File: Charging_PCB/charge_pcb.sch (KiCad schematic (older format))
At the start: 36 parts, among them J1 PCB_1, J2 Battery, J3 Power Switch, J4 24V Out, J5 Motor_Left, J6 Motor_Cutter, J7 Motor_Right, Q1 BC547C, Q2 IRF9540N, Q3 BC547C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

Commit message: Improve Q2 and Q4
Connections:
- net at D2.2 (K), R1.1, R4.1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: now also Q2.3 (S); no longer Q2.2 (D)
- net at D3.1 (K), U1.5 (IP-): now also Q2.2 (D); no longer Q2.3 (S)
- net at D5.2 (K), R6.1: now also Q4.3 (S); no longer Q4.2 (D)
- net at C1.1, J4.1, J5.1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: now also Q4.2 (D); no longer Q4.3 (S)
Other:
- moved on the sheet: Q2, Q4
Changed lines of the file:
@@
 Wire Wire Line
 	3500 2650 3500 2700
-Wire Wire Line
-	3500 2250 4400 2250
 Connection ~ 3500 2250
 $Comp
@@
 $EndComp
 Connection ~ 3500 3700
-Wire Wire Line
-	4400 2750 4850 2750
 Wire Wire Line
 	5500 3700 5500 3550
@@
 Wire Wire Line
 	4850 3000 4850 2750
-Connection ~ 4850 2750
 Wire Wire Line
 	4850 2750 5500 2750
@@
 L Transistor_FET:IRF9540N Q4
 U 1 1 60AF8999
-P 9000 2350
-F 0 "Q4" V 9342 2350 50  0000 C CNN
-F 1 "IRF9540N" V 9251 2350 50  0000 C CNN
-F 2 "Package_TO_SOT_THT:TO-220-3_Vertical" H 9200 2275 50  0001 L CIN
-F 3 "http://www.irf.com/product-info/datasheets/data/irf9540n.pdf" H 9000 2350 50  0001 L CNN
-	1    9000 2350
-	0    -1   -1   0
-$EndComp
-Wire Wire Line
-	7950 2550 7950 2950
-Wire Wire Line
-	9000 2550 7950 2550
-Connection ~ 7950 2550
+P 9000 2150
+F 0 "Q4" V 9342 2150 50  0000 C CNN
+F 1 "IRF9540N" V 9251 2150 50  0000 C CNN
+F 2 "Package_TO_SOT_THT:TO-220-3_Vertical" H 9200 2075 50  0001 L CIN
+F 3 "http://www.irf.com/product-info/datasheets/data/irf9540n.pdf" H 9000 2150 50  0001 L CNN
+	1    9000 2150
+	0    1    1    0
+$EndComp
+Wire Wire Line
+	7950 2550 7950 2600
 $Comp
 L Transistor_FET:IRF9540N Q2
 U 1 1 60B073F2
-P 4300 2550
-F 0 "Q2" H 4504 2596 50  0000 L CNN
-F 1 "IRF9540N" H 4504 2505 50  0000 L CNN
-F 2 "Package_TO_SOT_THT:TO-220-3_Vertical" H 4500 2475 50  0001 L CIN
-F 3 "http://www.irf.com/product-info/datasheets/data/irf9540n.pdf" H 4300 2550 50  0001 L CNN
-	1    4300 2550
-	1    0    0    -1
-$EndComp
-Wire Wire Line
-	4400 2250 4400 2350
-Wire Wire Line
-	4100 2650 4100 2550
+P 4500 2650
+F 0 "Q2" H 4704 2696 50  0000 L CNN
+F 1 "IRF9540N" H 4704 2605 50  0000 L CNN
+F 2 "Package_TO_SOT_THT:TO-220-3_Vertical" H 4700 2575 50  0001 L CIN
+F 3 "http://www.irf.com/product-info/datasheets/data/irf9540n.pdf" H 4500 2650 50  0001 L CNN
+	1    4500 2650
+	0    -1   -1   0
+$EndComp
 Wire Wire Line
 	6550 3050 6550 4650
@@
 Text GLabel 5500 6050 1    50   Output ~ 0
 pinBatteryVoltage
+Wire Wire Line
+	4700 2250 4700 2550
+Wire Wire Line
+	3500 2250 4700 2250
+Wire Wire Line
+	4300 2550 4300 2750
+Wire Wire Line
+	4300 2750 4850 2750
+Connection ~ 4850 2750
+Wire Wire Line
+	4100 2650 4100 2850
+Wire Wire Line
+	4100 2850 4500 2850
+Wire Wire Line
+	9000 1950 8400 1950
+Wire Wire Line
+	8400 1950 8400 2600
+Wire Wire Line
+	8400 2600 7950 2600
+Connection ~ 7950 2600
+Wire Wire Line
+	7950 2600 7950 2950
 $EndSCHEMATC

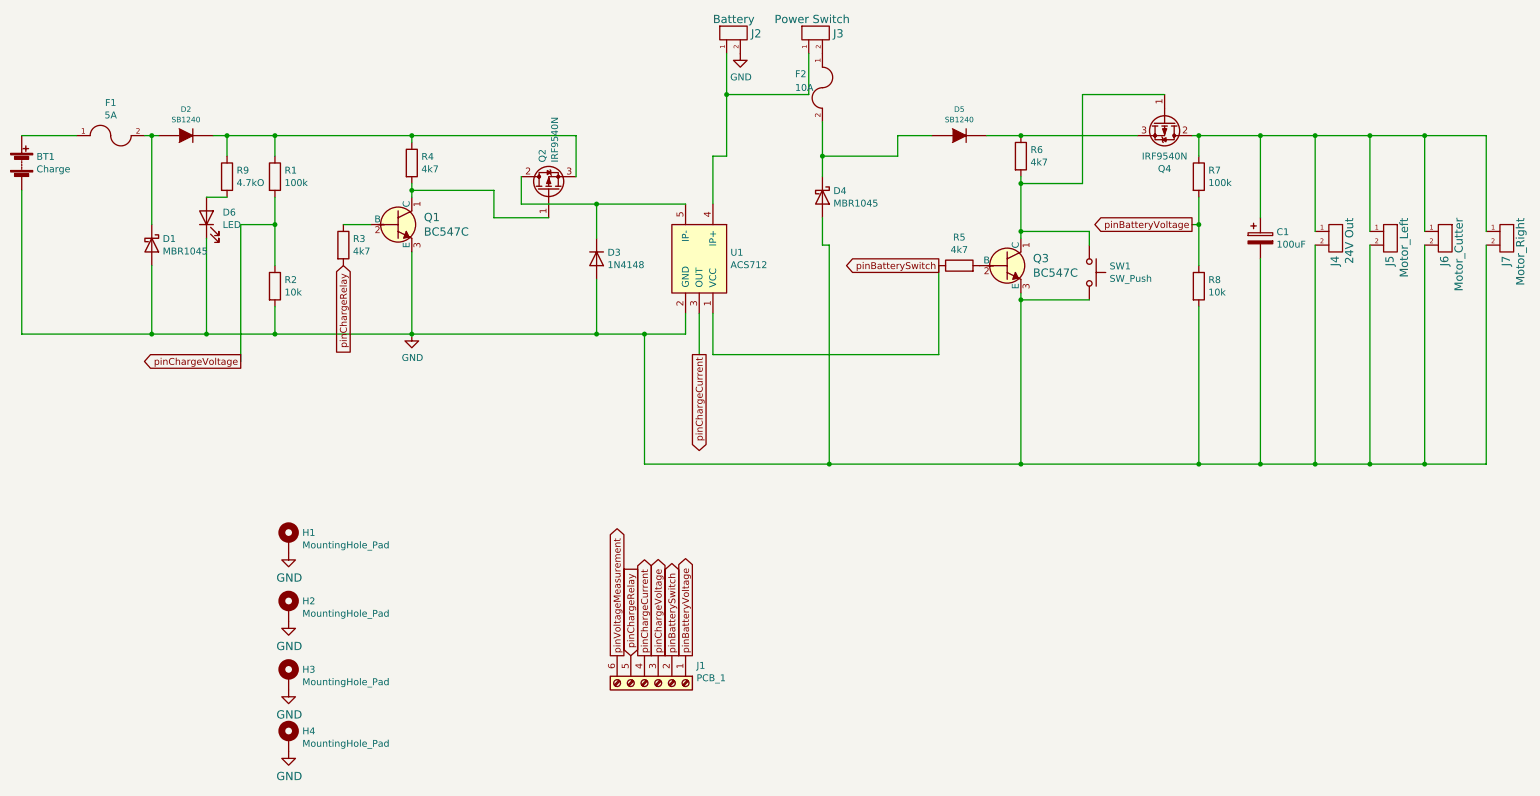
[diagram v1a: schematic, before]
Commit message: Rename pinChargeRelay to pinChargeEnable
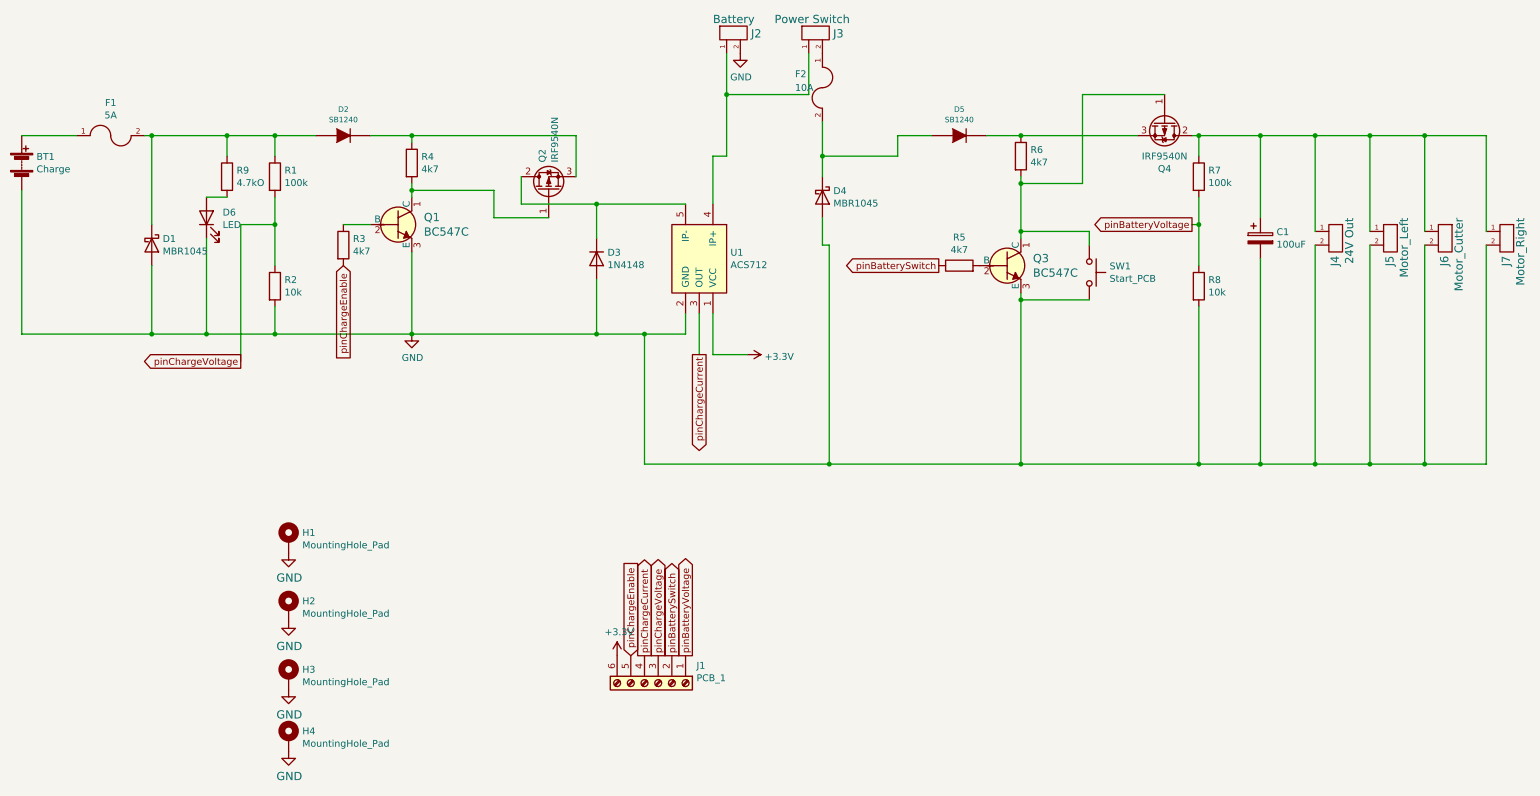
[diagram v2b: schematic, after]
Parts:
- SW1: value SW_Push -> Start_PCB
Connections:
- net pinBatterySwitch: no longer U1.1 (VCC)
- net at D1.1 (K), D2.1 (A), F1.2: now also R1.1, R9.1
- net at D2.2 (K), Q2.3 (S), R4.1: no longer R1.1, R9.1
- net pinChargeRelay renamed pinChargeEnable
- net pinVoltageMeasurement renamed +3V3
- net +3V3: now also U1.1 (VCC)
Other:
- moved on the sheet: D2
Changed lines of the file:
@@
 L Lötpad_2,5mm:DIODE D2
 U 1 1 6071023D
-P 1850 2250
-F 0 "D2" H 1850 2442 40  0000 C CNN
-F 1 "SB1240" H 1850 2366 40  0000 C CNN
-F 2 "Diode_THT:D_DO-41_SOD81_P10.16mm_Horizontal" H 1850 2250 60  0001 C CNN
-F 3 "" H 1850 2250 60  0000 C CNN
-	1    1850 2250
+P 3000 2250
+F 0 "D2" H 3000 2442 40  0000 C CNN
+F 1 "SB1240" H 3000 2366 40  0000 C CNN
+F 2 "Diode_THT:D_DO-41_SOD81_P10.16mm_Horizontal" H 3000 2250 60  0001 C CNN
+F 3 "" H 3000 2250 60  0000 C CNN
+	1    3000 2250
 	1    0    0    -1
 $EndComp
@@
 	3000 2900 3200 2900
 Text GLabel 3000 3200 3    50   Input ~ 0
-pinChargeRelay
+pinChargeEnable
 Wire Wire Line
 	3500 2650 4100 2650
@@
 Text GLabel 5400 6050 1    50   Output ~ 0
 pinBatterySwitch
-Text GLabel 5000 6050 1    50   Output ~ 0
-pinVoltageMeasurement
 Text GLabel 5200 6050 1    50   Output ~ 0
 pinChargeCurrent
 Text GLabel 5100 6050 1    50   Input ~ 0
-pinChargeRelay
+pinChargeEnable
 Wire Wire Line
 	650  2250 1050 2250
 Wire Wire Line
-	2500 2250 3500 2250
+	2500 2250 2800 2250
 $Comp
 L Lötpad_2,5mm:DIODE D5
@@
 Wire Wire Line
 	2250 2900 2500 2900
-Wire Wire Line
-	2050 2250 2150 2250
 Wire Wire Line
 	2150 2400 2150 2250
@@
 Wire Wire Line
 	650  3700 1600 3700
-Wire Wire Line
-	1600 2250 1650 2250
 $Comp
 L Switch:SW_Push SW1
@@
 P 8450 3250
 F 0 "SW1" V 8404 3398 50  0000 L CNN
-F 1 "SW_Push" V 8495 3398 50  0000 L CNN
+F 1 "Start_PCB" V 8495 3398 50  0000 L CNN
 F 2 "Connector_JST:JST_XH_B2B-XH-A_1x02_P2.50mm_Vertical" H 8450 3450 50  0001 C CNN
 F 3 "~" H 8450 3450 50  0001 C CNN
@@
 Wire Wire Line
 	7950 2950 7950 3000
-Wire Wire Line
-	7350 3850 7350 3200
-Wire Wire Line
-	5700 3850 7350 3850
 $Comp
 L Transistor_FET:IRF9540N Q4
@@
 Wire Wire Line
 	7950 2600 7950 2950
+$Comp
+L power:+3.3V #PWR?
+U 1 1 60A5AE88
+P 5000 6050
+F 0 "#PWR?" H 5000 5900 50  0001 C CNN
+F 1 "+3.3V" H 5015 6223 50  0000 C CNN
+F 2 "" H 5000 6050 50  0001 C CNN
+F 3 "" H 5000 6050 50  0001 C CNN
+	1    5000 6050
+	1    0    0    -1
+$EndComp
+$Comp
+L power:+3.3V #PWR?
+U 1 1 60A5B730
+P 5950 3850
+F 0 "#PWR?" H 5950 3700 50  0001 C CNN
+F 1 "+3.3V" V 5965 3978 50  0000 L CNN
+F 2 "" H 5950 3850 50  0001 C CNN
+F 3 "" H 5950 3850 50  0001 C CNN
+	1    5950 3850
+	0    1    1    0
+$EndComp
+Wire Wire Line
+	5700 3850 5950 3850
+Wire Wire Line
+	3200 2250 3500 2250
+Wire Wire Line
+	1600 2250 2150 2250
 $EndSCHEMATC

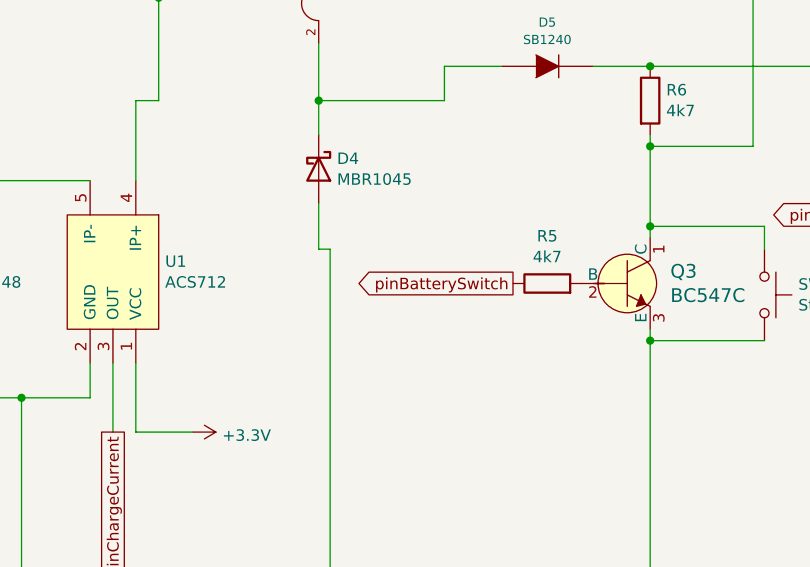
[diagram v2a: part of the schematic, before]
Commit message: Board Route
Board routed and make Gerber Files
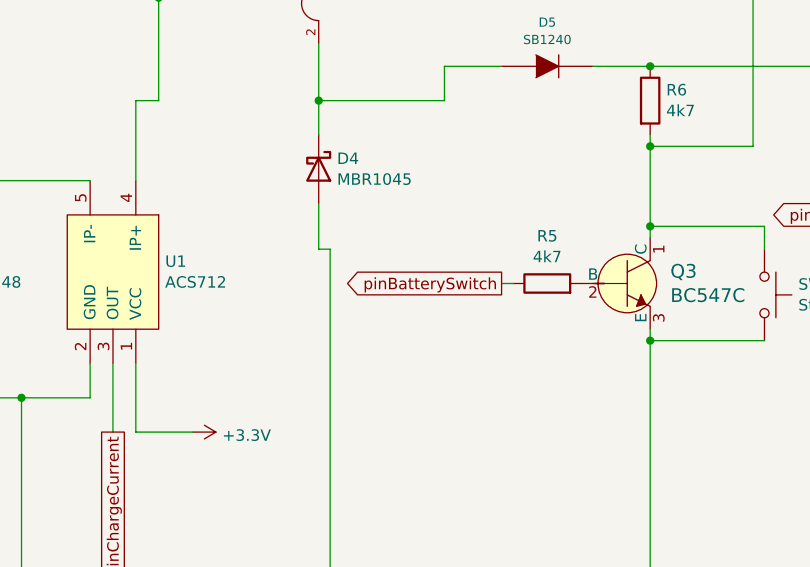
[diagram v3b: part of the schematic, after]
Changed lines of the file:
@@
 	1    0    0    -1
 $EndComp
-Text GLabel 7350 3200 0    50   Output ~ 0
+Text GLabel 7300 3200 0    50   Output ~ 0
 pinBatterySwitch
 $Comp
@@
 Wire Wire Line
 	1600 2250 2150 2250
+Wire Wire Line
+	7300 3200 7350 3200
 $EndSCHEMATC

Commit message: Add Bernards Changes
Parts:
- removed SW1: Start_PCB, Connector_JST:JST_XH_B2B-XH-A_1x02_P2.50mm_Vertical, symbol Switch:SW_Push
- added D8: SB1240, Diode_THT:D_DO-41_SOD81_P10.16mm_Horizontal, symbol charge_pcb-rescue:DIODE-Lötpad_2,5mm
- added J8: Start, Connector_JST:JST_XH_B2B-XH-A_1x02_P2.50mm_Vertical, symbol Connector:Screw_Terminal_01x02
- added J9: 24V out, TerminalBlock:TerminalBlock_bornier-2_P5.08mm, symbol charge_pcb-rescue:HEADER_2-Zimprich
- added R10, R11: 2k2, Resistor_THT:R_Axial_DIN0207_L6.3mm_D2.5mm_P7.62mm_Horizontal, symbol Device:R
- D2, D5: symbol Lötpad_2,5mm:DIODE -> charge_pcb-rescue:DIODE-Lötpad_2,5mm
- F1, F2: symbol Zimprich:FUSE -> charge_pcb-rescue:FUSE-Zimprich
- J1: footprint Connector_PinHeader_2.54mm:PinHeader_1x06_P2.54mm_Vertical -> Connector_JST:JST_XH_B6B-XH-A_1x06_P2.50mm_Vertical
- J2, J3, J4, J6: symbol Zimprich:HEADER_2 -> charge_pcb-rescue:HEADER_2-Zimprich
- J5: value Motor_Left -> Motor_Drive; symbol Zimprich:HEADER_2 -> charge_pcb-rescue:HEADER_2-Zimprich
- J7: value Motor_Right -> 24V Out; symbol Zimprich:HEADER_2 -> charge_pcb-rescue:HEADER_2-Zimprich
- Q1, Q3: symbol dk_Transistors-Bipolar-BJT-Single:BC548BTA -> charge_pcb-rescue:BC548BTA-dk_Transistors-Bipolar-BJT-Single
- U1: value ACS712 -> INA169; symbol Lötpad_2,5mm:ACS712 -> charge_pcb-rescue:ACS712-Lötpad_2,5mm
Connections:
- net GND: now also J8.2 (Pin_2), J9.2, R10.2, R11.2
- net pinBatterySwitch: now also R10.1
- net pinChargeEnable: now also R11.1
- net at D2.2 (K), R4.1: now also Q2.2 (D); no longer Q2.3 (S)
- net at D3.1 (K), U1.5 (IP-): now also Q2.3 (S); no longer Q2.2 (D)
- net at Q3.1 (C), Q4.1 (G), R6.2: now also J8.1 (Pin_1)
- net at D5.2 (K), R6.1: now also Q4.2 (D); no longer Q4.3 (S)
- net at C1.1, J4.1, J7.1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: now also Q4.3 (S), D8.1 (A), J9.1; no longer J5.1, J6.1, Q4.2 (D)
- new net: D8.2 (K), J5.1, J6.1
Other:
- moved on the sheet: C1, D1, D2, D4, D6, J1, J4, J5, J7, Q3, R1, R2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
